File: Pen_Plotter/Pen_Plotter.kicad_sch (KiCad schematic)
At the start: 37 parts, among them J1 USB4125-GF-A_REVA2, J2 PinHeader_01x05_P2.54mm_Verti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, J3 PinHeader_01x05_P2.54mm_Verti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, J4 Conn_02x03_Counter_Clockwise, J5 PinHeader_01x02_P2.54mm_Verti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, J6 PinHeader_01x02_P2.54mm_Verti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, J7 PinHeader_01x03_P2.54mm_Verti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, SW1 Switch_Tactile_Omron, SW2 Switch_Tactile_Omron, U1 ESP32-WROOM-32E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

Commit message: First PCB Final - Problems with RX-TX
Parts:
- C3: value C_1206 -> 1uF
- C4, C5: value 22uF -> 10uF
- C7, C8: value C_1206 -> 0.1uF
- R10: value R_1206 -> 10K
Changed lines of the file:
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@@
 			)
 		)
-		(property "Value" "22uF"
+		(property "Value" "10uF"
 			(at 269.24 39.3699 0)
 			(effects
@@
 			)
 		)
-		(property "Value" "22uF"
+		(property "Value" "10uF"
 			(at 246.38 39.3699 0)
 			(effects
@@
 			)
 		)
-		(property "Value" "R_1206"
+		(property "Value" "10K"
 			(at 48.26 135.8899 0)
 			(effects
@@
 			)
 		)
-		(property "Value" "C_1206"
+		(property "Value" "0.1uF"
 			(at 328.93 36.8299 0)
 			(effects
@@
 			)
 		)
-		(property "Value" "C_1206"
+		(property "Value" "0.1uF"
 			(at 109.22 52.0699 0)
 			(effects
@@
 			)
 		)
-		(property "Value" "C_1206"
+		(property "Value" "1uF"
 			(at 261.62 132.08 90)
 			(effects

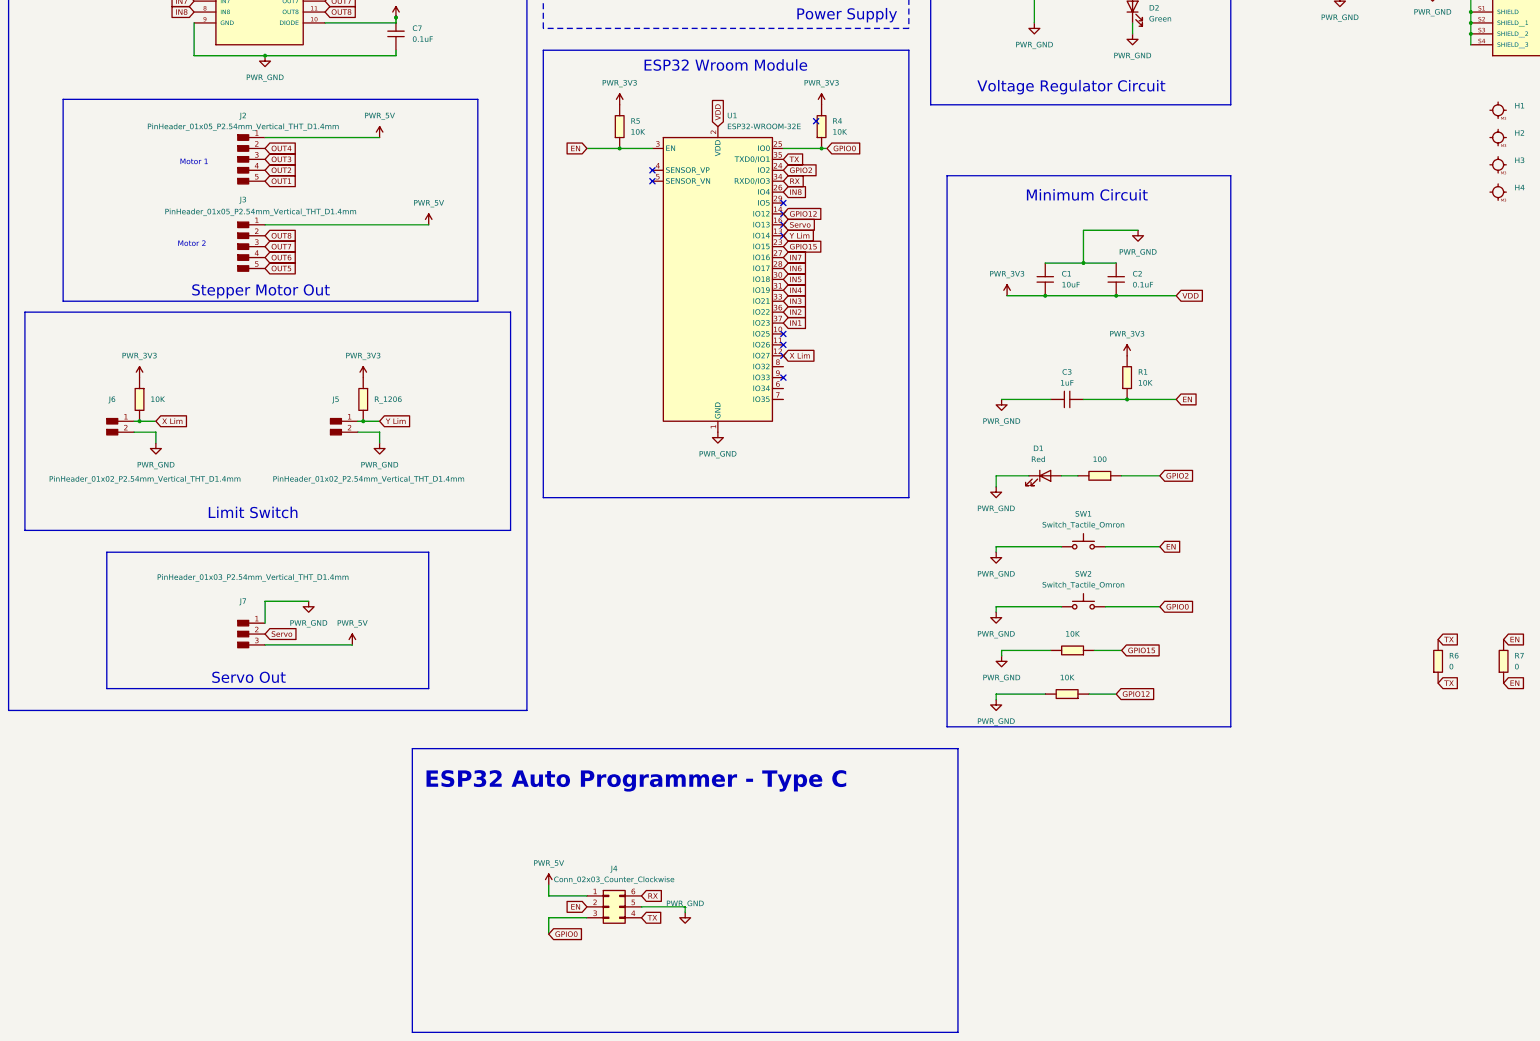
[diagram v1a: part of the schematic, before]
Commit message: PCB _ TX and RX Corrected
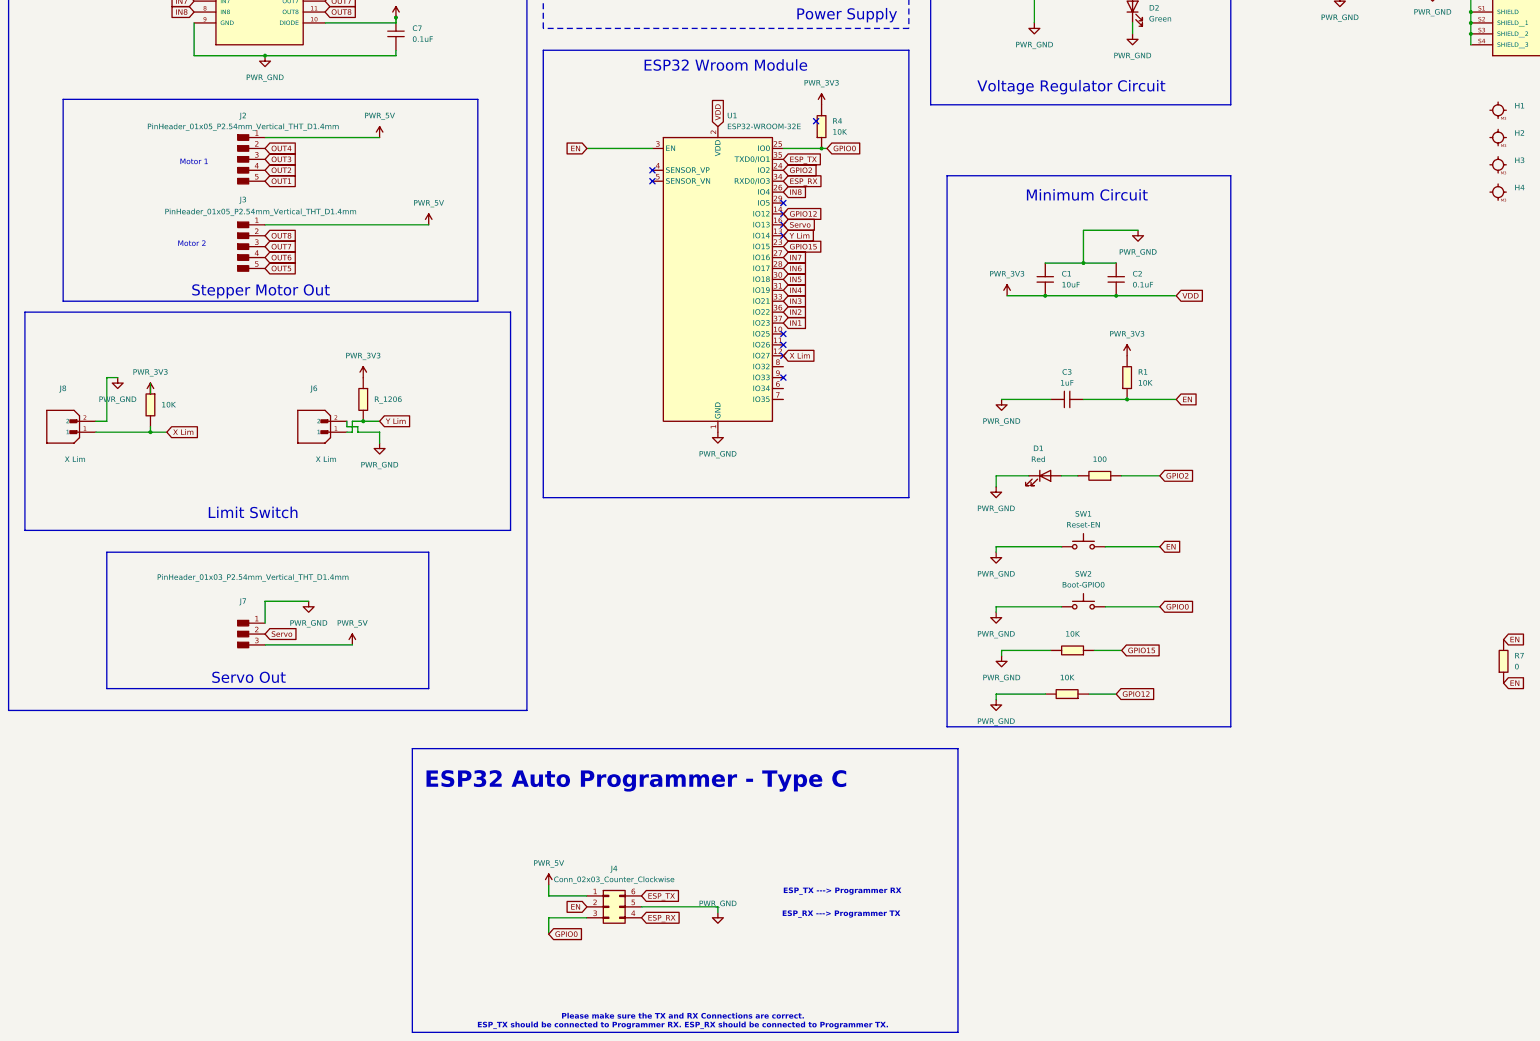
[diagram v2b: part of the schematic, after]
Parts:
- removed J5, J6: PinHeader_01x02_P2.54mm_Vertical_THT_D1.4mm, fab:PinHeader_01x02_P2.54mm_Vertical_THT_D1.4mm, symbol fab:PinHeader_01x02_P2.54mm_Vertical_THT_D1.4mm
- removed R5: 10K, fab:R_1206, symbol fab:R_1206
- removed R6: 0, fab:R_1206, symbol fab:R_1206
- added J6, J8: X Lim, B2B-XH-A_LF__SN_:JST_B2B-XH-A_LF__SN_, symbol B2B-XH-A_LF__SN_:B2B-XH-A_LF__SN_
- SW1: value Switch_Tactile_Omron -> Reset-EN
- SW2: value Switch_Tactile_Omron -> Boot-GPIO0
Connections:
- net PWR_GND: now also J6.2, J8.2
- net X Lim: now also J8.1
- net Y Lim: now also J6.1
- net RX renamed ESP_RX
- net ESP_RX: now also J4.4 (Pin_4); no longer J4.6 (Pin_6)
- net TX renamed ESP_TX
- net ESP_TX: now also J4.6 (Pin_6); no longer J4.4 (Pin_4)
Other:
- note added: "ESP_RX ---> Programmer TX"
- note added: "ESP_TX ---> Programmer RX"
- note added: "Please make sure the TX and RX Connections are correct. ESP_TX should be connected to Programmer RX. ESP_RX should be connected to Programmer TX."
